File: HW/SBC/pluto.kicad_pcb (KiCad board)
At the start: 2 copper layers, 149.9 x 90.2 mm, 41 parts, among them J1 Serial Port, J2 CONN_02X07, J3 CONN_02X07, J4 POWER IN, J5 Expansion Port, Q1 DS1813, SW1 RESET, U1 WD65C02_, U10 74LS138, U11 LM7805CT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

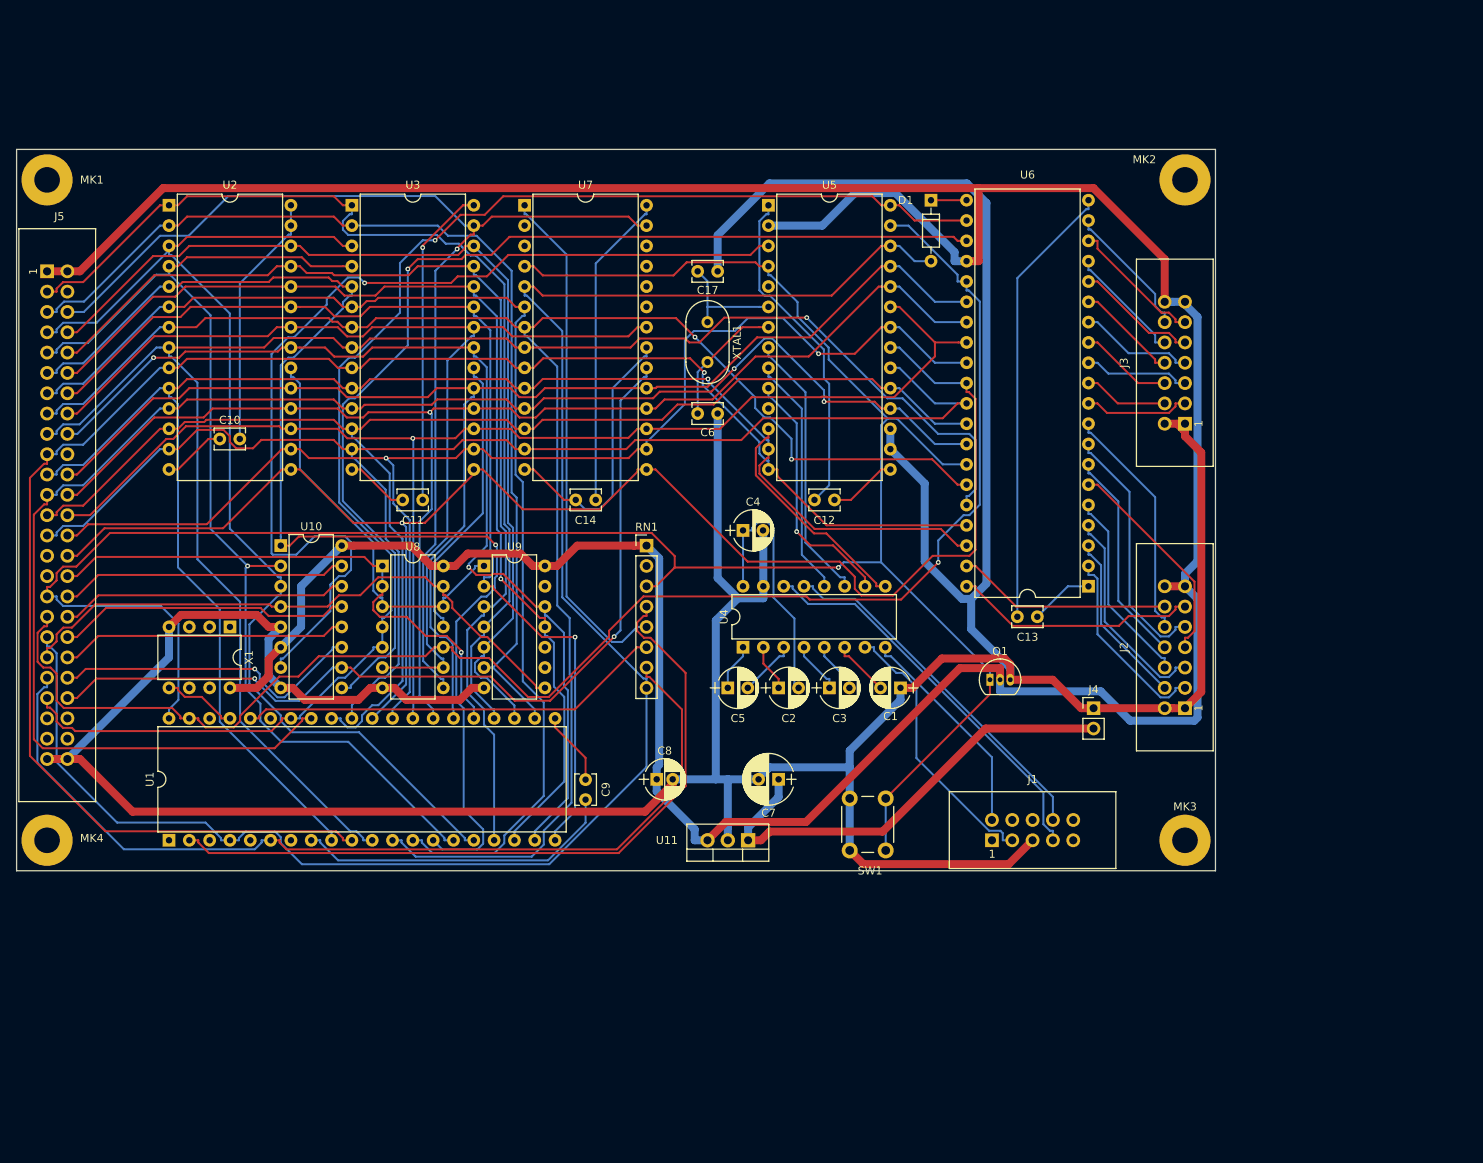
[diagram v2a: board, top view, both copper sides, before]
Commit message: New SBC PCB. Started to split pluto_kernel.asm into bios, monitor and miniassembler/disassembler. Various other updates.
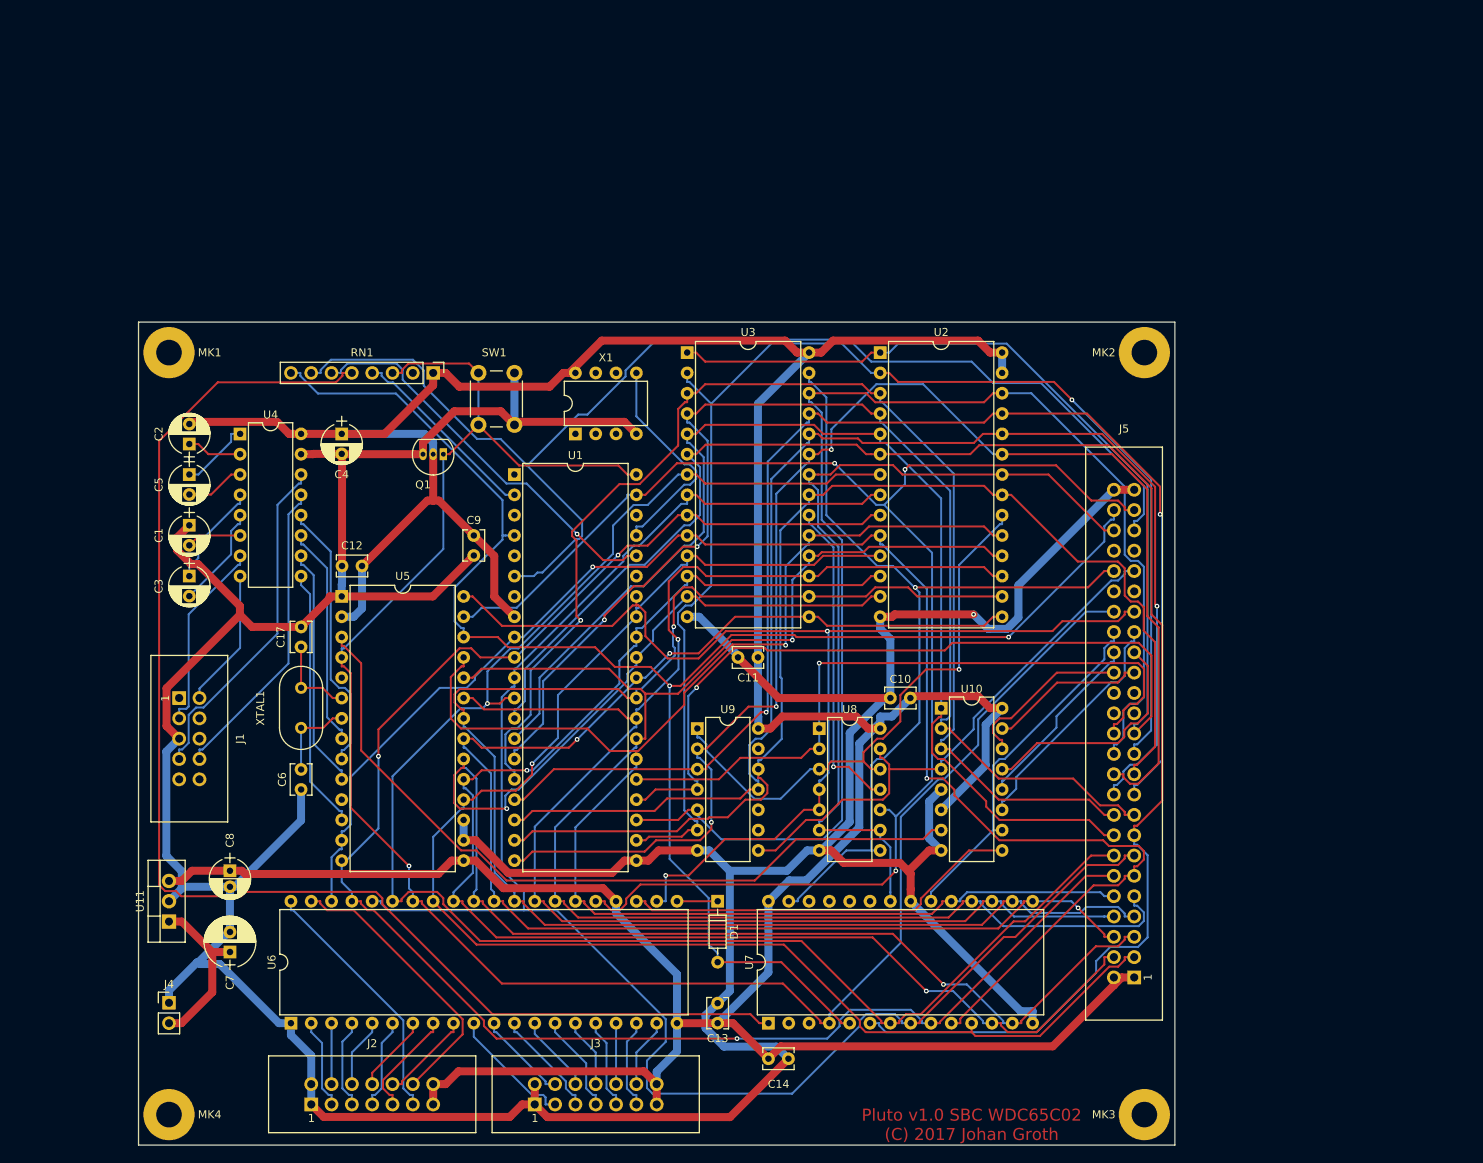
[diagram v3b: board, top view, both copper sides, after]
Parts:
- moved J5 162.0 mm to (176.5, 132.7), turned to 90 degrees
- moved J4 121.3 mm to (55.9, 135.9)
- moved J2 119.9 mm to (73.7, 148.6), turned to 0 degrees
- moved J3 117.7 mm to (101.6, 148.6), turned to 0 degrees
- moved U6 113.7 mm to (71.1, 138.4), turned to 90 degrees
- moved U7 106.7 mm to (130.8, 138.4), turned to 90 degrees
- moved J1 103.1 mm to (57.1, 97.8), turned to 270 degrees
- moved D1 91.6 mm to (124.5, 123.2)
- moved C1 91.2 mm to (58.4, 76.2), turned to 270 degrees
- moved U2 90.8 mm to (144.8, 54.6)
- moved C10 89.9 mm to (146.1, 97.8)
- moved U10 85.0 mm to (152.4, 99.1)
- moved C3 81.2 mm to (58.4, 82.5), turned to 270 degrees
- moved C2 79.7 mm to (58.4, 66.0), turned to 90 degrees
- moved Q1 73.9 mm to (90.2, 67.3), turned to 180 degrees
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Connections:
- C10 pad 1: Net-(C10-Pad1) -> GND
- C10 pad 2: Net-(C10-Pad2) -> VCC
- C11 pad 1: Net-(C11-Pad1) -> GND
- C11 pad 2: Net-(C11-Pad2) -> VCC
- C12 pad 1: Net-(C12-Pad1) -> VCC
- C12 pad 2: Net-(C12-Pad2) -> GND
- C13 pad 1: Net-(C13-Pad1) -> VCC
- C13 pad 2: Net-(C13-Pad2) -> GND
- C14 pad 1: Net-(C14-Pad1) -> VCC
- C14 pad 2: Net-(C14-Pad2) -> GND
- C2 pad 2: Net-(C2-Pad2) -> VCC
- C4 pad 1: Net-(C2-Pad2) -> VCC
- C9 pad 1: Net-(C9-Pad1) -> VCC
- C9 pad 2: Net-(C9-Pad2) -> GND
- J1 pad 1: (no net) -> Net-(J1-Pad1)
- J1 pad 10: (no net) -> Net-(J1-Pad10)
- J1 pad 4: (no net) -> Net-(J1-Pad4)
- J1 pad 6: (no net) -> Net-(J1-Pad6)
- J1 pad 9: (no net) -> Net-(J1-Pad9)
- J5 pad 10: A8 -> D7
- J5 pad 11: A5 -> A0
- J5 pad 12: A9 -> A1
- J5 pad 13: A4 -> A2
- J5 pad 14: A11 -> A3
- J5 pad 15: A3 -> A4
- J5 pad 16: ~MRD -> A5
- J5 pad 17: A2 -> A6
- J5 pad 18: A10 -> A7
- J5 pad 19: A1 -> A8
- J5 pad 20: (no net) -> A9
- J5 pad 21: A0 -> A10
- J5 pad 22: D7 -> A11
- J5 pad 23: D0 -> A12
- J5 pad 24: D6 -> A13
- J5 pad 25: D1 -> A14
- J5 pad 26: D5 -> A15
- J5 pad 27: D2 -> Net-(J5-Pad27)
- J5 pad 28: D4 -> Net-(J5-Pad28)
- J5 pad 29: (no net) -> Net-(J5-Pad29)
- J5 pad 3: A14 -> D0
- J5 pad 30: D3 -> Net-(J5-Pad30)
- J5 pad 31: (no net) -> ~7F0X
- J5 pad 32: A15 -> ~7F2X
- J5 pad 33: ~RES -> ~7F4X
- J5 pad 34: ~7F0X -> ~7F6X
- J5 pad 35: CLK -> ~7F8X
- J5 pad 36: ~7F2X -> ~7FAX
- J5 pad 37: ~IRQ -> R/~W
- J5 pad 38: ~7F4X -> ~RES
- J5 pad 39: ~IOSEL -> Net-(J5-Pad39)
- J5 pad 4: (no net) -> D1
- J5 pad 40: ~7F6X -> Net-(J5-Pad40)
- J5 pad 41: ~NMI -> ~IOSEL
- J5 pad 42: ~7F8X -> ~MWR
- J5 pad 43: R/~W -> Net-(J5-Pad43)
- J5 pad 44: ~7FAX -> Net-(J5-Pad44)
- J5 pad 45: (no net) -> ~NMI
- J5 pad 46: (no net) -> ~MRD
- J5 pad 47: (no net) -> CLK
- J5 pad 48: (no net) -> ~IRQ
- J5 pad 5: A12 -> D2
- J5 pad 6: ~MWR -> D3
- J5 pad 7: A7 -> D4
- J5 pad 8: A13 -> D5
- J5 pad 9: A6 -> D6
- RN1 pad 2: (no net) -> Net-(RN1-Pad2)
- U1 pad 1: (no net) -> Net-(U1-Pad1)
- U1 pad 21: Net-(C9-Pad2) -> GND
- U1 pad 3: (no net) -> Net-(U1-Pad3)
- U1 pad 35: (no net) -> Net-(U1-Pad35)
- U1 pad 38: (no net) -> Net-(U1-Pad38)
- U1 pad 5: (no net) -> Net-(U1-Pad5)
- U1 pad 7: (no net) -> Net-(U1-Pad7)
- U1 pad 8: Net-(C9-Pad1) -> VCC
- U2 pad 14: Net-(C10-Pad1) -> GND
- U2 pad 27: Net-(C10-Pad2) -> VCC
- U2 pad 28: Net-(C10-Pad2) -> VCC
- U3 pad 14: Net-(C11-Pad1) -> GND
- U3 pad 28: Net-(C11-Pad2) -> VCC
- U4 pad 16: Net-(C2-Pad2) -> VCC
- U5 pad 1: Net-(C12-Pad2) -> GND
- U5 pad 11: (no net) -> Net-(U5-Pad11)
- U5 pad 15: Net-(C12-Pad1) -> VCC
- U5 pad 5: (no net) -> Net-(U5-Pad5)
- U6 pad 1: Net-(C13-Pad2) -> GND
- U6 pad 20: Net-(C13-Pad1) -> VCC
- U7 pad 14: Net-(C14-Pad2) -> GND
- U7 pad 21: Net-(C14-Pad2) -> GND
- U7 pad 23: (no net) -> Net-(U7-Pad23)
- U7 pad 24: (no net) -> Net-(U7-Pad24)
- U7 pad 26: (no net) -> Net-(U7-Pad26)
- U7 pad 28: Net-(C14-Pad1) -> VCC
- X1 pad 1: (no net) -> Net-(X1-Pad1)
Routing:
- net ~PWR: track 64.3 -> 167.5 mm
- net ~7FCX: track 134.5 -> 49.9 mm, vias 1 -> 0
- net VCC: track 436.4 -> 506.1 mm
- net RDY: track 92.4 -> 24.3 mm
- net ~7FAX: track 112.8 -> 44.8 mm, vias 2 -> 0
- net A14: track 128.4 -> 191.1 mm, vias 0 -> 1
- net A4: track 150.2 -> 207.1 mm
- net Net-(C13-Pad1): track 55.9 -> 0.00 mm
- net A13: track 122.1 -> 166.9 mm
- net A11: track 133.8 -> 177.7 mm, vias 1 -> 3
- net A12: track 126.8 -> 170.6 mm, vias 0 -> 1
- net Net-(C12-Pad2): track 42.2 -> 0.00 mm
- net ~RES: track 281.3 -> 239.2 mm
- net Net-(C9-Pad1): track 40.3 -> 0.00 mm
- net Net-(C11-Pad2): track 40.3 -> 0.00 mm, vias 1 -> 0
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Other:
- board size 149.9 x 90.2 mm -> 129.5 x 102.9 mm
- board text added: "Pluto v1.0 SBC WDC65C02 (C) 2017 Johan Groth"

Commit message: New board layout with decoupling caps in the right place. Updates to the RTC code (IRQ still doesn't work).
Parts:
- moved C9 29.0 mm to (105.4, 104.1), turned to 0 degrees
- moved C14 14.0 mm to (139.7, 132.1), turned to 90 degrees
- moved C13 11.4 mm to (114.9, 132.1)
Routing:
- net GND: track 538.9 -> 0.00 mm, vias 1 -> 0
- net VCC: track 506.1 -> 0.00 mm
- net ~RES: track 239.2 -> 0.00 mm, vias 1 -> 0
- net A2: track 216.8 -> 0.00 mm
- net A1: track 213.6 -> 0.00 mm, vias 3 -> 0
- net A3: track 208.3 -> 0.00 mm, vias 1 -> 0
- net A4: track 207.1 -> 0.00 mm
- net ~IRQ: track 206.7 -> 0.00 mm, vias 2 -> 0
- net A0: track 195.9 -> 0.00 mm, vias 2 -> 0
- net D6: track 194.8 -> 0.00 mm, vias 1 -> 0
- net D4: track 192.8 -> 0.00 mm, vias 1 -> 0
- net CLK: track 192.7 -> 0.00 mm, vias 3 -> 0
- net A14: track 191.1 -> 0.00 mm, vias 1 -> 0
- net D7: track 190.4 -> 0.00 mm, vias 1 -> 0
- net D5: track 190.4 -> 0.00 mm, vias 1 -> 0
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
